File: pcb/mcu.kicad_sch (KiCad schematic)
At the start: 29 parts, among them J1 SWD+UART, SW1 BOOT, SW2 RESET, SW3 USER, U1 RP2350A, U2 W25Q128JVS, Y1 12MHz

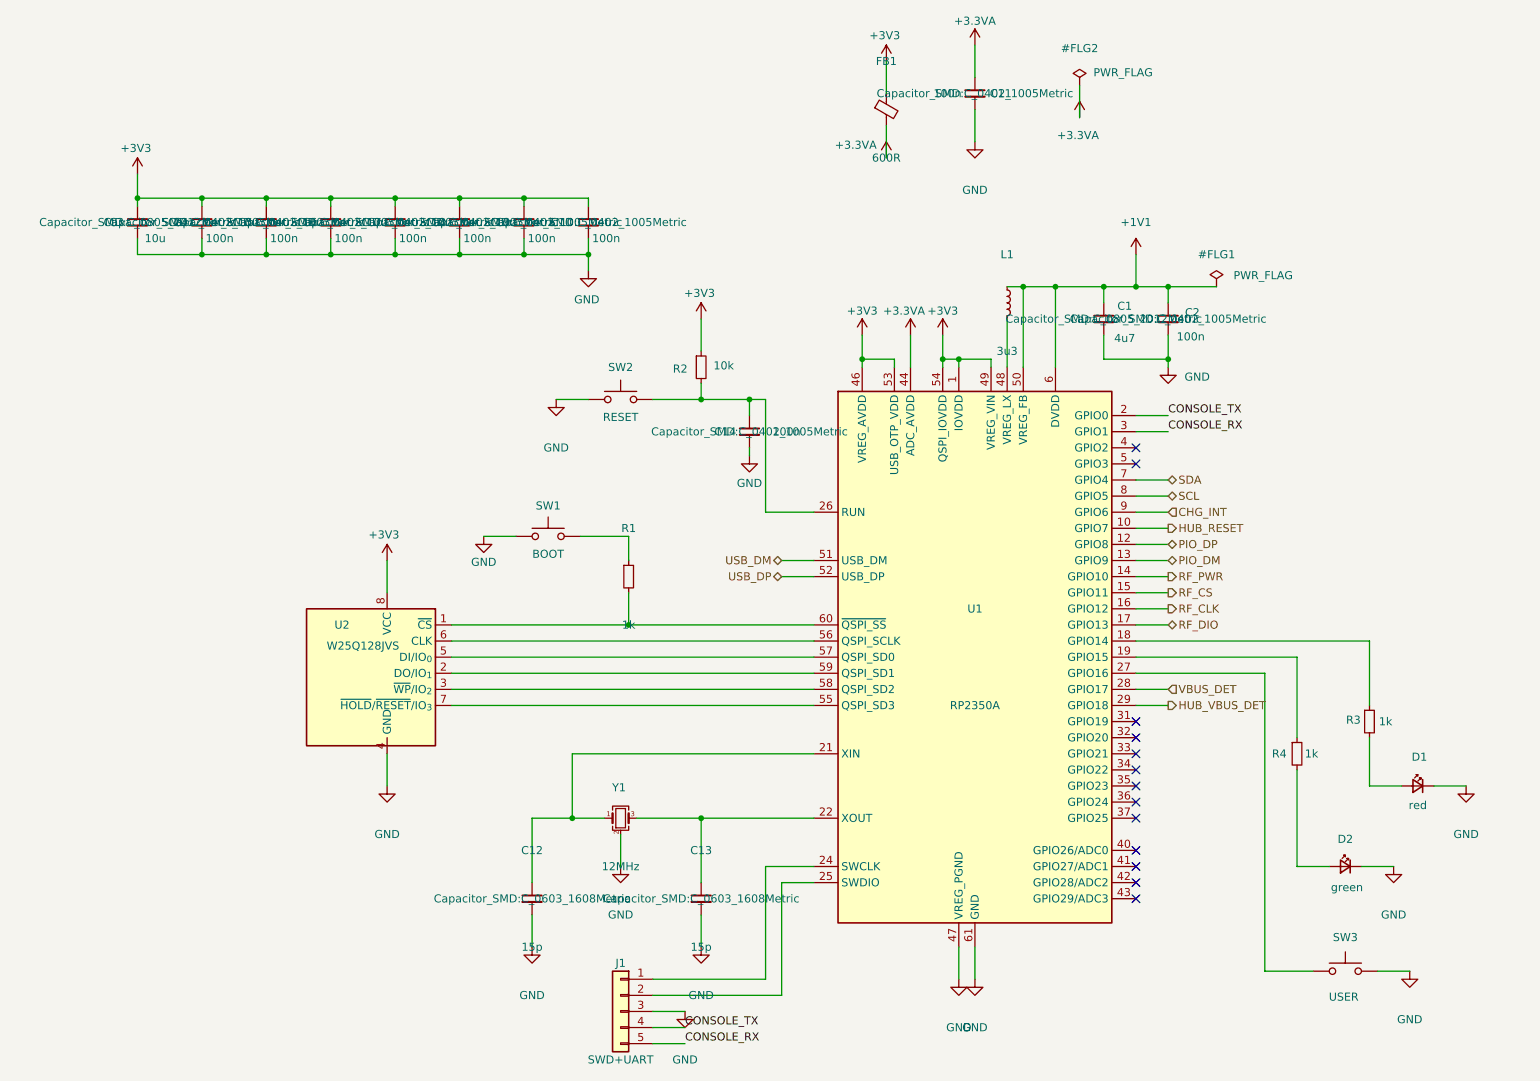
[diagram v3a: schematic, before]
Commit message: assign the footprints, and take the radio module's from its vendor
132 of the 135 parts now carry a footprint. Most follow from the package, the capacitors' follow
from the bias calculation, and the resistors are 0603 rather than 0402 because the board has room,
the first one runs bare on a bench, and a part you can get a probe or an iron onto is worth more
there than the millimetre it saves.

The radio module nearly went in hand-drawn. It has no footprint in any stock library, so the
obvious move was to draw one from the dimension drawing in its datasheet; the pitch, pad size and
pad length read off cleanly, but where each pad sits along its edge did not, and what I had was
inference from where things appeared in a rendered figure rather than a stated number. Raspberry Pi
publish a KiCad symbol and footprint, so that is what is fitted, in a project footprint library
beside the project symbol library. The figure agreed on everything it stated plainly, which says
nothing about the parts it did not.

Taking the official symbol also checked this project's hand-drawn one against theirs. All 21 pins
agree. Four carry different names -- their DI and DO, their nIRQ and WL_ON -- and nothing else
differs, so the pin numbering derived from the module's table is confirmed against its author
rather than merely self-consistent.

Four packages are fitted provisionally and are recorded as such, because what is unsettled about
them is invisible: the processor, the hub, the 3.3V converter and the power sink are in packages
whose library entries differ only in the size of the pad under the part. Body, pitch and pin count
are right; the pad is the nearest variant and wants checking against each vendor's land pattern,
since too small costs thermal performance and too large can wick the part off its pins.

Three parts are deliberately left without one. For the remaining inductors the footprint is the
part -- pad geometry differs between vendors at the same nominal size -- so choosing an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
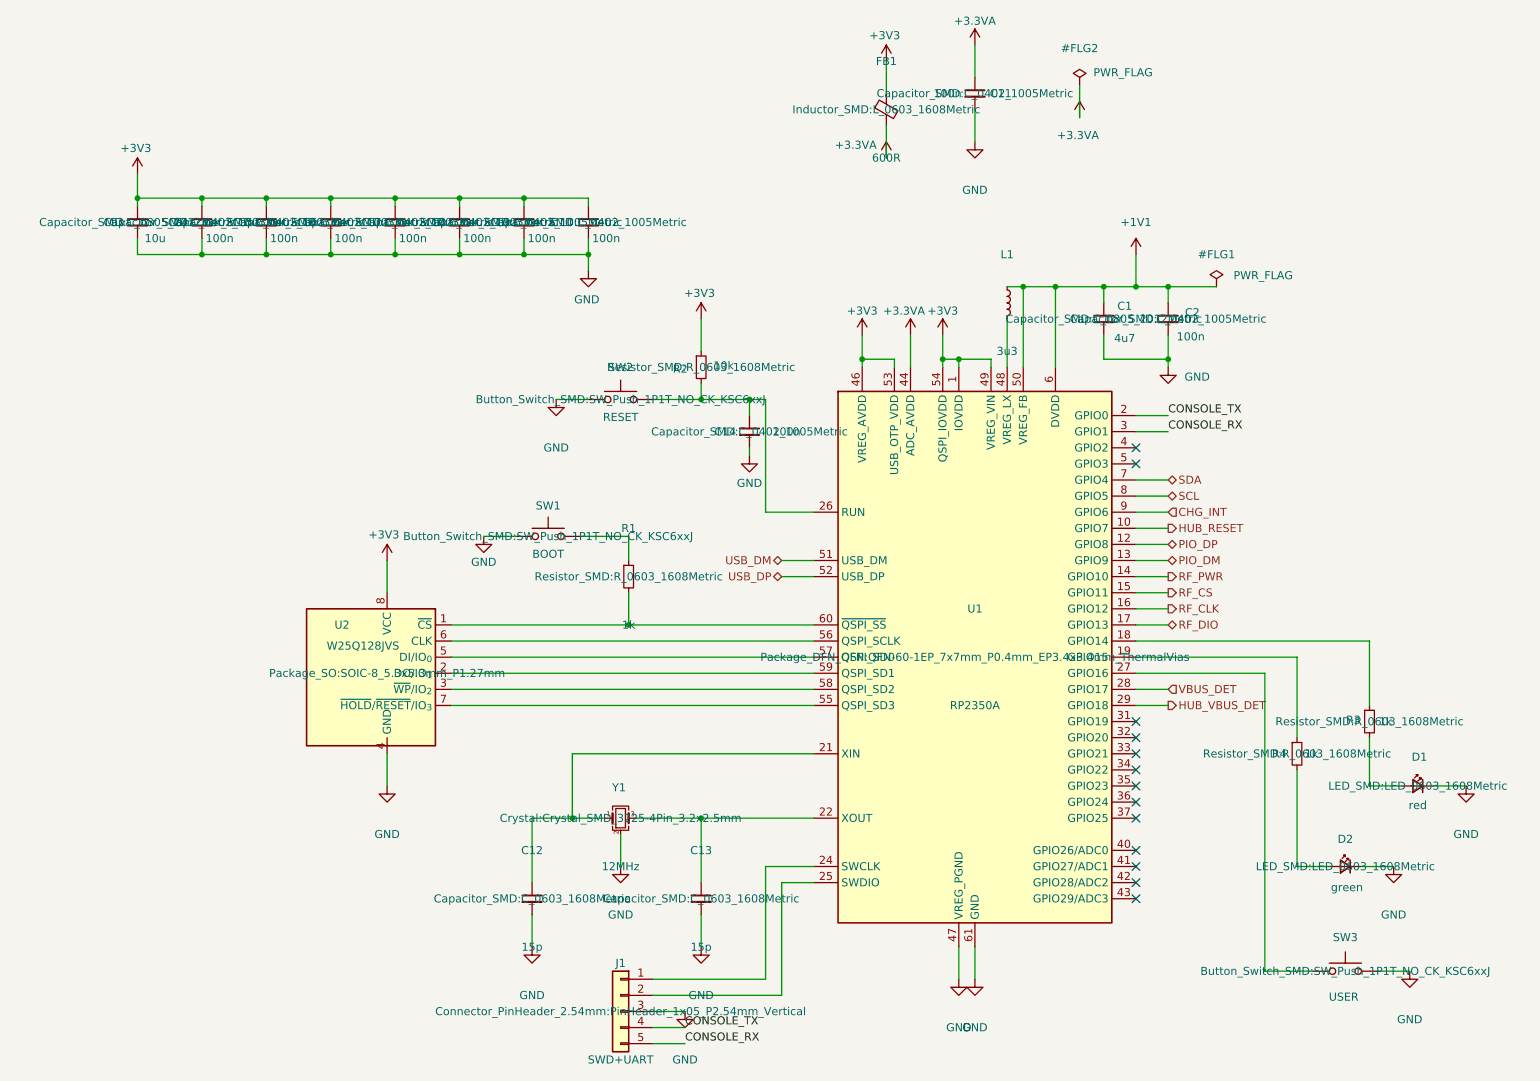
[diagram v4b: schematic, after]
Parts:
- D1, D2: footprint (none) -> LED_SMD:LED_0603_1608Metric
- FB1: footprint (none) -> Inductor_SMD:L_0603_1608Metric
- J1: footprint (none) -> Connector_PinHeader_2.54mm:PinHeader_1x05_P2.54mm_Vertical
- R1, R2, R3, R4: footprint (none) -> Resistor_SMD:R_0603_1608Metric
- SW1, SW2, SW3: footprint (none) -> Button_Switch_SMD:SW_Push_1P1T_NO_CK_KSC6xxJ
- U1: footprint (none) -> Package_DFN_QFN:QFN-60-1EP_7x7mm_P0.4mm_EP3.4x3.4mm_ThermalVias
- U2: footprint (none) -> Package_SO:SOIC-8_5.3x5.3mm_P1.27mm
- Y1: footprint (none) -> Crystal:Crystal_SMD_3225-4Pin_3.2x2.5mm
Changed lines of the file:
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@@
 			)
 		)
-		(property "Footprint" ""
+		(property "Footprint" "Button_Switch_SMD:SW_Push_1P1T_NO_CK_KSC6xxJ"
 			(at 135.89 120.65 0)
 			(show_name no)
@@
 			)
 		)
-		(property "Footprint" ""
+		(property "Footprint" "Package_DFN_QFN:QFN-60-1EP_7x7mm_P0.4mm_EP3.4x3.4mm_ThermalVias"
 			(at 203.2 139.7 0)
 			(show_name no)
@@
 			)
 		)
-		(property "Footprint" ""
+		(property "Footprint" "Resistor_SMD:R_0603_1608Metric"
 			(at 254 154.94 0)
 			(show_name no)
@@
 			)
 		)
-		(property "Footprint" ""
+		(property "Footprint" "Button_Switch_SMD:SW_Push_1P1T_NO_CK_KSC6xxJ"
 			(at 147.32 99.06 0)
 			(show_name no)
@@
 			)
 		)
-		(property "Footprint" ""
+		(property "Footprint" "Resistor_SMD:R_0603_1608Metric"
 			(at 148.59 127 0)
 			(show_name no)
@@
 			)
 		)
-		(property "Footprint" ""
+		(property "Footprint" "Connector_PinHeader_2.54mm:PinHeader_1x05_P2.54mm_Vertical"
 			(at 147.32 195.58 0)
 			(show_name no)
@@
 			)
 		)
-		(property "Footprint" ""
+		(property "Footprint" "Inductor_SMD:L_0603_1608Metric"
 			(at 189.23 53.34 0)
 			(show_name no)
@@
 			)
 		)
-		(property "Footprint" ""
+		(property "Footprint" "Resistor_SMD:R_0603_1608Metric"
 			(at 265.43 149.86 0)
 			(show_name no)
@@
 			)
 		)
-		(property "Footprint" ""
+		(property "Footprint" "Button_Switch_SMD:SW_Push_1P1T_NO_CK_KSC6xxJ"
 			(at 261.62 189.23 0)
 			(show_name no)
@@
 			)
 		)
-		(property "Footprint" ""
+		(property "Footprint" "Resistor_SMD:R_0603_1608Metric"
 			(at 160.02 93.98 0)
 			(show_name no)
@@
 			)
 		)
-		(property "Footprint" ""
+		(property "Footprint" "Package_SO:SOIC-8_5.3x5.3mm_P1.27mm"
 			(at 110.49 142.24 0)
 			(show_name no)
@@
 			)
 		)
-		(property "Footprint" ""
+		(property "Footprint" "Crystal:Crystal_SMD_3225-4Pin_3.2x2.5mm"
 			(at 147.32 165.1 0)
 			(show_name no)
@@
 			)
 		)
-		(property "Footprint" ""
+		(property "Footprint" "LED_SMD:LED_0603_1608Metric"
 			(at 273.05 160.02 0)
 			(show_name no)
@@
 			)
 		)
-		(property "Footprint" ""
+		(property "Footprint" "LED_SMD:LED_0603_1608Metric"
 			(at 261.62 172.72 0)
 			(show_name no)

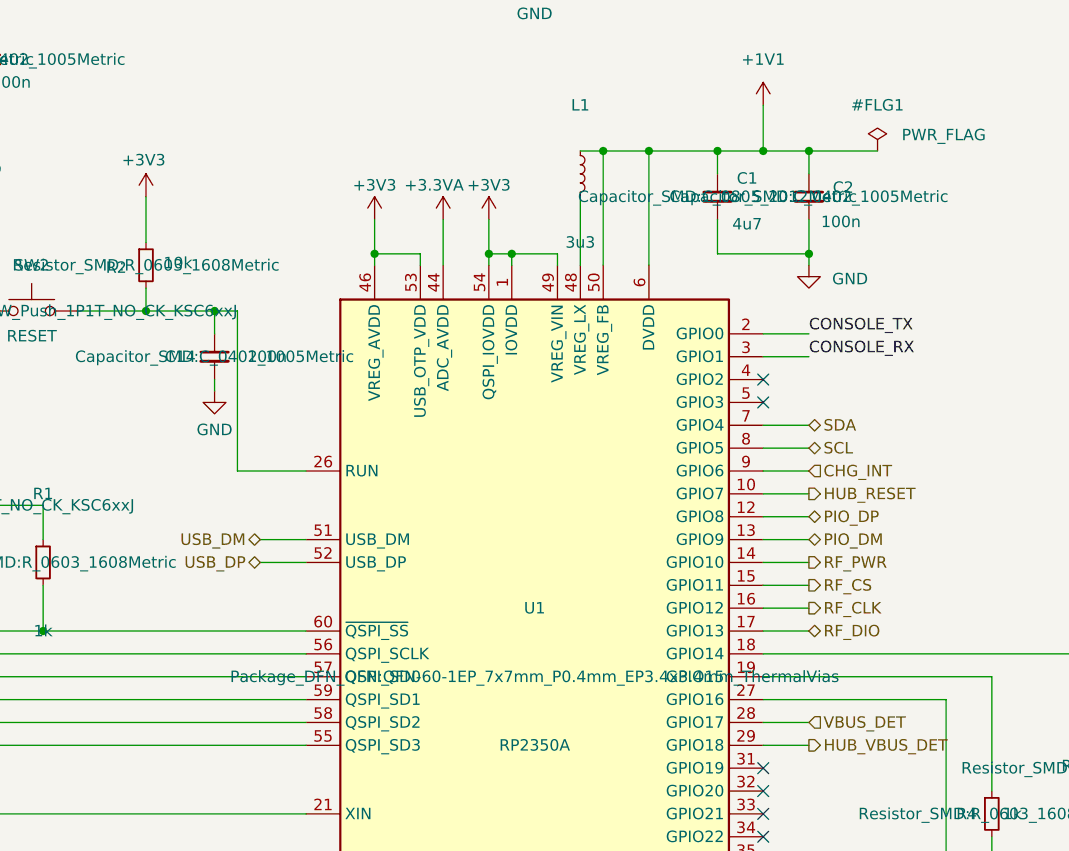
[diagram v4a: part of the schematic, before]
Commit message: select the inductors, and take two footprints from the processor's reference design
Four parts, and two of them are the same one. The core regulator takes the part its own vendor
names. The charger takes a Coilcraft XGL4030-102MEC, and the 3.3V converter takes the same part
again: it needs only 3A where the charger needs 7, but one part number, one land pattern and one
thing to stock is worth more than the margin it wastes, and it has lower resistance than the part
that converter's vendor suggests. The 5V boost keeps the Wurth part from its vendor's own list.

Saturation quoted against an inductance droop rather than as a single number is what made these
comparable. The charger needs about 7A at worst. The first part considered reaches that only at a
30% droop, which would feed back into more ripple and a higher peak again; the one chosen is still
holding 80% of its inductance there, for a millimetre of extra height in the same 4mm footprint and
lower resistance as well.

Two footprints now come from the processor vendor's published reference design, which is MIT
licensed and carried in with the notice that licence requires. One is the core inductor's, which no
stock library had. The other is the processor's own land pattern, and that settles one of the four
packages fitted provisionally: the pad under it is no longer the nearest library variant but the
pattern its maker lays out. Three provisional packages remain, and so does the land pattern for the
two Coilcraft parts, which is a single drawing covering both.

133 of 135 parts now carry a footprint.

Co-Authored-By: Claude Opus 5 (1M context) <noreply@anthropic.com>
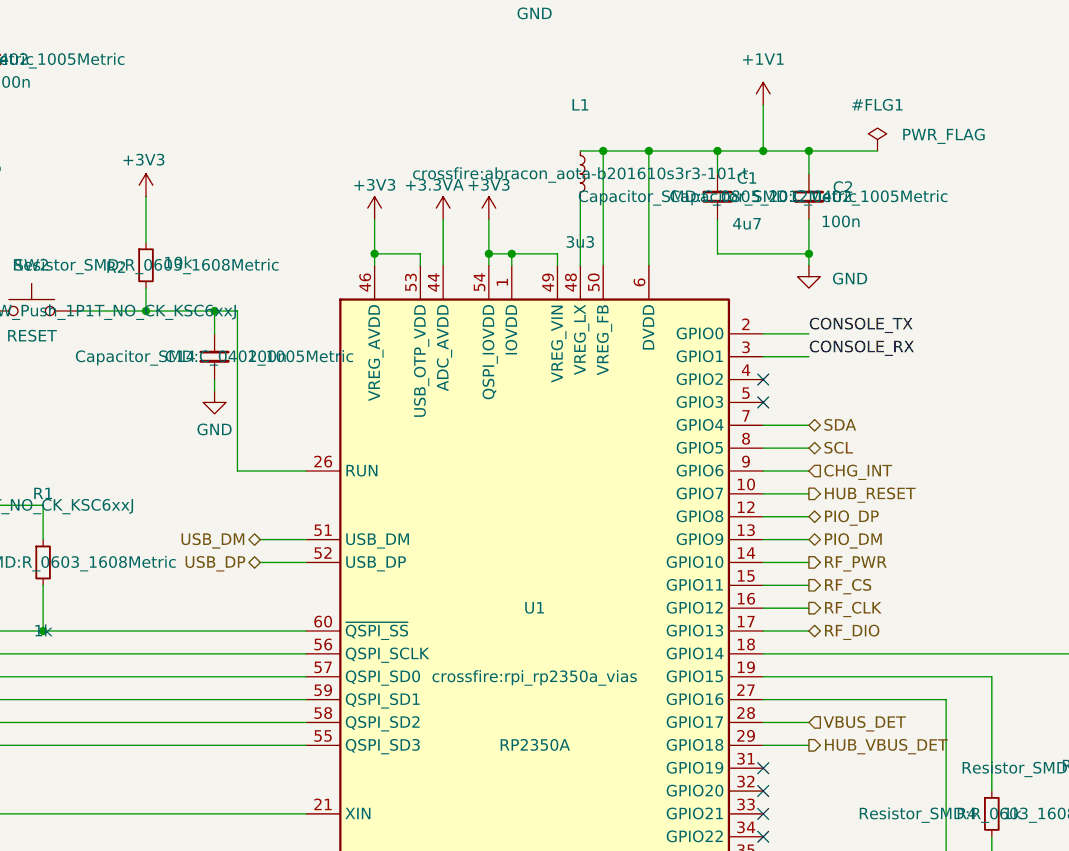
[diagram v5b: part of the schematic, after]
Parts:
- L1: footprint (none) -> crossfire:abracon_aota-b201610s3r3-101-t; MPN (none) -> Abracon AOTA-B201610S3R3-101-T
- U1: footprint Package_DFN_QFN:QFN-60-1EP_7x7mm_P0.4mm_EP3.4x3.4mm_ThermalVias -> crossfire:rpi_rp2350a_vias
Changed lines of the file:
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@@
 			)
 		)
-		(property "Footprint" "Package_DFN_QFN:QFN-60-1EP_7x7mm_P0.4mm_EP3.4x3.4mm_ThermalVias"
+		(property "Footprint" "crossfire:rpi_rp2350a_vias"
 			(at 203.2 139.7 0)
 			(show_name no)
@@
 			)
 		)
+		(property "MPN" "Abracon AOTA-B201610S3R3-101-T"
+			(at 208.28 91.44 0)
+			(show_name no)
+			(do_not_autoplace no)
+			(effects
+				(font
+					(size 1.27 1.27)
+				)
+				(hide yes)
+			)
+		)
 		(property "Tolerance" "20%"
 			(at 208.28 91.44 0)
@@
 			)
 		)
-		(property "Footprint" ""
+		(property "Footprint" "crossfire:abracon_aota-b201610s3r3-101-t"
 			(at 208.28 83.82 0)
 			(show_name no)
